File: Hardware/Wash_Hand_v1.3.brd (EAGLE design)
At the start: 71.1 x 48.3 mm, 64 parts, among them IC1 LM358D, IC2 LP298XS, IC3 4050D, J1 I2C, J2 ICSP, J3 SPI, J5 EXT_VCC, J6 6_PIN_SERIAL_CABLEPTH, Q1 16.0 Mhz, U1 328P

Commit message: Board/Schematic: Update to v1.3a.2
Signed-off-by: Konrad Rzeszutek Wilk <konrad@kernel.org>
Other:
- board text added: "v1.3a.2"
- board text removed: "v1.3a.1"
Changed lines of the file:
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@@
 <circle x="6.35" y="37.592" radius="0.254" width="0.254" layer="25"/>
 <circle x="6.35" y="37.592" radius="0.567959375" width="0.1524" layer="25"/>
-<text x="21.336" y="19.558" size="1.778" layer="26" ratio="14" rot="MR0">v1.3a.1</text>
+<text x="21.336" y="19.558" size="1.778" layer="26" ratio="14" rot="MR0">v1.3a.2</text>
 <text x="56.134" y="15.494" size="1.016" layer="25" ratio="14">#
 [  ]
@@
 <element name="MICROSD" library="darnok_microsd" package="114-00841-68" value="114-00841-68" x="9.94" y="29.718" smashed="yes" rot="R270"/>
 <element name="FRAME1" library="darnok_frame" package="REVISION_TEXT" value="" x="54.356" y="22.606" smashed="yes">
-<attribute name="REVISION" value="v1.3a.1" x="54.356" y="22.606" size="1.778" layer="27" display="off"/>
+<attribute name="REVISION" value="v1.3a.2" x="54.356" y="22.606" size="1.778" layer="27" display="off"/>
 </element>
 <element name="FRAME2" library="darnok_frame" package="REVISION_TEXT" value="" x="18.542" y="19.812" smashed="yes" rot="MR0">
-<attribute name="REVISION" value="v1.3a.1" x="18.542" y="19.812" size="1.778" layer="28" rot="MR0" display="off"/>
+<attribute name="REVISION" value="v1.3a.2" x="18.542" y="19.812" size="1.778" layer="28" rot="MR0" display="off"/>
 </element>
 </elements>

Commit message: Board/Schematic: Change 22pf to 10pf
Which makes the crystal work..

Signed-off-by: Konrad Rzeszutek Wilk <konrad@kernel.org>
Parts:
- C1, C2: value 22pF -> 10pF
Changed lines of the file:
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@@
 </autorouter>
 <elements>
-<element name="C1" library="SparkFun-Capacitors" library_urn="urn:adsk.eagle:library:510" package="1206" package3d_urn="urn:adsk.eagle:package:37426/1" value="22pF" x="25.654" y="18.288" smashed="yes" rot="R270">
+<element name="C1" library="SparkFun-Capacitors" library_urn="urn:adsk.eagle:library:510" package="1206" package3d_urn="urn:adsk.eagle:package:37426/1" value="10pF" x="25.654" y="18.288" smashed="yes" rot="R270">
 <attribute name="NAME" x="26.67" y="18.288" size="0.6096" layer="25" font="vector" ratio="20" rot="R270" align="bottom-center"/>
 <attribute name="PROD_ID" value="CAP-10057" x="-28.956" y="-4.572" size="1.778" layer="27" rot="R270" display="off"/>
 <attribute name="VALUE" value="10uF" x="24.638" y="18.288" size="0.6096" layer="27" font="vector" ratio="20" rot="R270" align="top-center"/>
 </element>
-<element name="C2" library="SparkFun-Capacitors" library_urn="urn:adsk.eagle:library:510" package="1206" package3d_urn="urn:adsk.eagle:package:37426/1" value="22pF" x="29.718" y="18.288" smashed="yes" rot="R90">
+<element name="C2" library="SparkFun-Capacitors" library_urn="urn:adsk.eagle:library:510" package="1206" package3d_urn="urn:adsk.eagle:package:37426/1" value="10pF" x="29.718" y="18.288" smashed="yes" rot="R90">
 <attribute name="NAME" x="28.702" y="18.288" size="0.6096" layer="25" font="vector" ratio="20" rot="R90" align="bottom-center"/>
 <attribute name="PROD_ID" value="CAP-10057" x="84.328" y="46.228" size="1.778" layer="27" rot="R90" display="off"/>

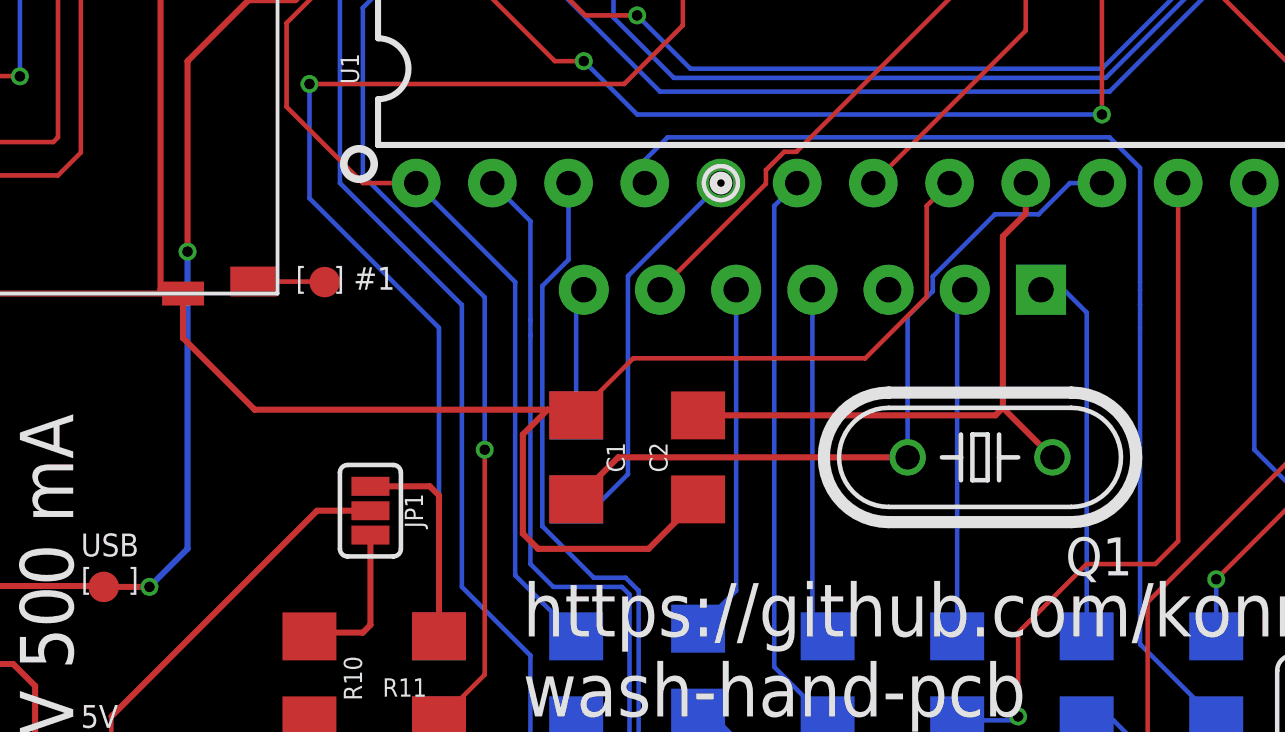
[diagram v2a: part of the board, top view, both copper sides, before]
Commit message: Board/Schematic: Fix the 16MHz/10pF capacitors.
The way they are were in the schematic looked right.
Two capacitors off the crystal. Both capacitors go to
ground. Except that what Eagle decided it should be was:

XTAL1         XTAL2
|             |
+--[CRYSTAL]--+
	 [CAP]
	  |
	 [CAP]
	  |
	 [GND]

Instead of the:

XTAL1         XTAL2
|             |
+--[CRYSTAL]--+
[CAP]        [CAP]
|             |
\------+------/
 [GND]

This fixes it.

Signed-off-by: Konrad Rzeszutek Wilk <konrad@kernel.org>
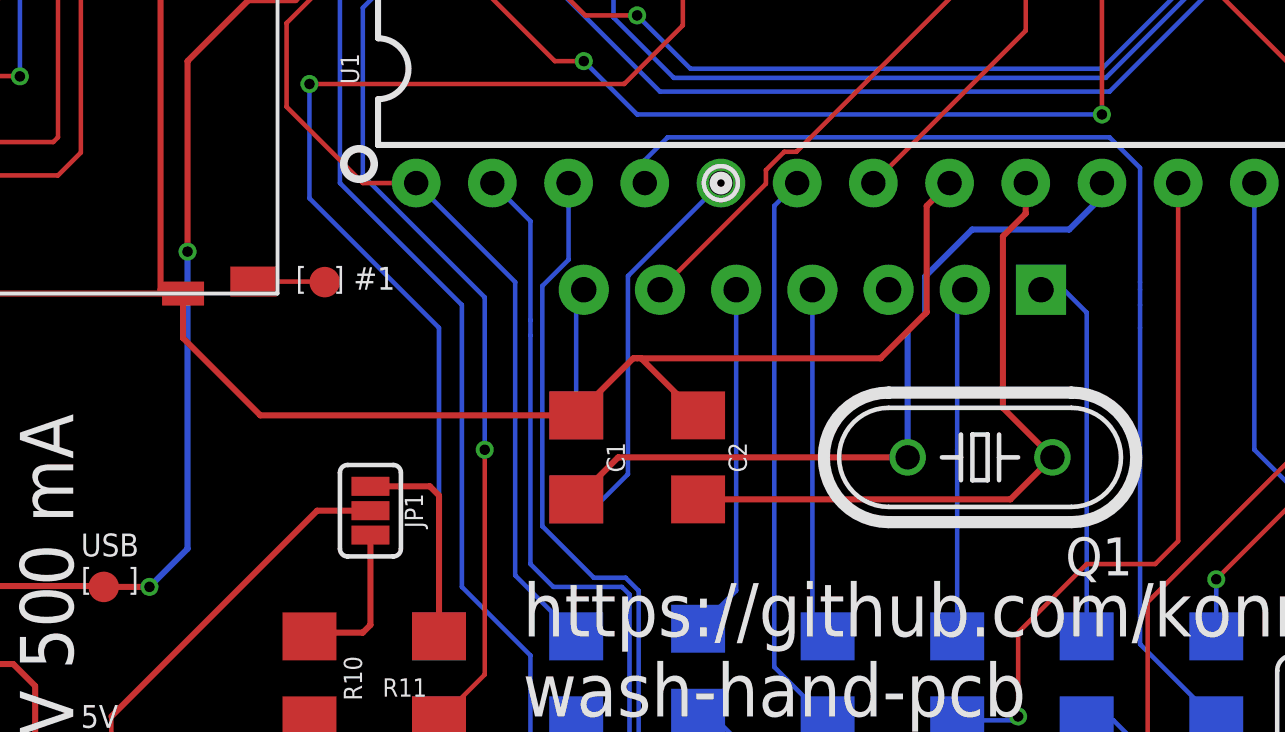
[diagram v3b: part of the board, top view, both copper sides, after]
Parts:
- turned C2 to 270 degrees
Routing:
- net 0: track 346.2 -> 338.0 mm
- net XTAL1: track 20.4 -> 22.5 mm
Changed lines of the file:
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@@
 <attribute name="VALUE" value="10uF" x="24.638" y="18.288" size="0.6096" layer="27" font="vector" ratio="20" rot="R270" align="top-center"/>
 </element>
-<element name="C2" library="SparkFun-Capacitors" library_urn="urn:adsk.eagle:library:510" package="1206" package3d_urn="urn:adsk.eagle:package:37426/1" value="10pF" x="29.718" y="18.288" smashed="yes" rot="R90">
-<attribute name="NAME" x="28.702" y="18.288" size="0.6096" layer="25" font="vector" ratio="20" rot="R90" align="bottom-center"/>
-<attribute name="PROD_ID" value="CAP-10057" x="84.328" y="46.228" size="1.778" layer="27" rot="R90" display="off"/>
-<attribute name="VALUE" value="10uF" x="30.734" y="18.288" size="0.6096" layer="27" font="vector" ratio="20" rot="R90" align="top-center"/>
+<element name="C2" library="SparkFun-Capacitors" library_urn="urn:adsk.eagle:library:510" package="1206" package3d_urn="urn:adsk.eagle:package:37426/1" value="10pF" x="29.718" y="18.288" smashed="yes" rot="R270">
+<attribute name="NAME" x="30.734" y="18.288" size="0.6096" layer="25" font="vector" ratio="20" rot="R270" align="bottom-center"/>
+<attribute name="PROD_ID" value="CAP-10057" x="-24.892" y="-9.652" size="1.778" layer="27" rot="R270" display="off"/>
+<attribute name="VALUE" value="10uF" x="28.702" y="18.288" size="0.6096" layer="27" font="vector" ratio="20" rot="R270" align="top-center"/>
 </element>
 <element name="J" library="SparkFun-Connectors" library_urn="urn:adsk.eagle:library:513" package="1X03" package3d_urn="urn:adsk.eagle:package:38063/1" value="D0    GND  VCC  ," x="63.5" y="8.89" smashed="yes" rot="MR180">
@@
 <signal name="0">
 <contactref element="U$4" pad="5"/>
-<contactref element="C2" pad="1"/>
-<contactref element="C1" pad="1"/>
 <contactref element="J" pad="2"/>
 <contactref element="J5" pad="1"/>
@@
 <wire x1="11.938" y1="23.748" x2="4.7" y2="23.748" width="0.2032" layer="1"/>
 <wire x1="4.7" y1="23.748" x2="4.699" y2="23.749" width="0.2032" layer="1"/>
-<wire x1="14.938840625" y1="19.877" x2="12.55" y2="22.265840625" width="0.2032" layer="1"/>
 <wire x1="12.55" y1="23.748" x2="12.55" y2="22.265840625" width="0.2032" layer="1"/>
 <wire x1="10.033" y1="45.7454" x2="8.763" y2="45.7454" width="0.2032" layer="1"/>
@@
 <wire x1="56.8198" y1="1.1938" x2="47.8282" y2="1.1938" width="0.2032" layer="1"/>
 <wire x1="47.8282" y1="1.1938" x2="45.974" y2="3.048" width="0.2032" layer="1"/>
-<wire x1="14.938840625" y1="19.877" x2="24.703" y2="19.877" width="0.2032" layer="1"/>
-<wire x1="25.465" y1="19.877" x2="25.654" y2="19.688" width="0.2032" layer="1"/>
-<wire x1="29.718" y1="16.888" x2="28.07" y2="15.24" width="0.2032" layer="1"/>
-<wire x1="28.07" y1="15.24" x2="24.384" y2="15.24" width="0.2032" layer="1"/>
-<wire x1="24.384" y1="15.24" x2="23.876" y2="15.748" width="0.2032" layer="1"/>
-<wire x1="23.876" y1="15.748" x2="23.876" y2="19.05" width="0.2032" layer="1"/>
-<wire x1="23.876" y1="19.05" x2="24.703" y2="19.877" width="0.2032" layer="1"/>
-<wire x1="24.703" y1="19.877" x2="25.465" y2="19.877" width="0.2032" layer="1"/>
 <wire x1="45.466" y1="45.85" x2="46.606" y2="45.85" width="0.2032" layer="1"/>
 <wire x1="46.606" y1="45.85" x2="47.752" y2="44.704" width="0.2032" layer="1"/>
@@
 <wire x1="7.874" y1="43.18" x2="10.16" y2="43.18" width="0.2032" layer="1"/>
 <wire x1="4.2" y1="39.506" x2="7.874" y2="43.18" width="0.2032" layer="1"/>
-<wire x1="25.654" y1="19.688" x2="27.556" y2="21.59" width="0.1524" layer="1"/>
-<wire x1="35.2906875" y1="21.59" x2="37.338" y2="23.6373125" width="0.1524" layer="1"/>
-<wire x1="37.338" y1="26.67" x2="38.1" y2="27.432" width="0.1524" layer="1"/>
-<wire x1="27.556" y1="21.59" x2="35.2906875" y2="21.59" width="0.1524" layer="1"/>
-<wire x1="37.338" y1="23.6373125" x2="37.338" y2="26.67" width="0.1524" layer="1"/>
+<wire x1="35.7986875" y1="21.59" x2="37.338" y2="23.1293125" width="0.2032" layer="1"/>
+<wire x1="37.338" y1="26.67" x2="38.1" y2="27.432" width="0.2032" layer="1"/>
+<wire x1="27.816" y1="21.59" x2="35.7986875" y2="21.59" width="0.2032" layer="1"/>
+<wire x1="37.338" y1="23.1293125" x2="37.338" y2="26.67" width="0.2032" layer="1"/>
 <wire x1="16.44076875" y1="39.37" x2="16.316153125" y2="39.494615625" width="0.2032" layer="1"/>
 <wire x1="7.62" y1="4.064" x2="8.636" y2="3.048" width="0.2032" layer="1"/>
@@
 <wire x1="67.37" y1="30.353" x2="69.342" y2="32.325" width="0.2032" layer="1"/>
 <wire x1="69.342" y1="32.325" x2="69.342" y2="34.544" width="0.2032" layer="1"/>
+<contactref element="C2" pad="1"/>
+<contactref element="C1" pad="1"/>
+<wire x1="15.127840625" y1="19.688" x2="25.654" y2="19.688" width="0.2032" layer="1"/>
+<wire x1="12.55" y1="22.265840625" x2="15.127840625" y2="19.688" width="0.2032" layer="1"/>
+<wire x1="25.654" y1="19.688" x2="27.556" y2="21.59" width="0.2032" layer="1"/>
+<wire x1="27.556" y1="21.59" x2="27.686" y2="21.59" width="0.2032" layer="1"/>
+<wire x1="29.718" y1="19.688" x2="27.816" y2="21.59" width="0.2032" layer="1"/>
+<wire x1="27.816" y1="21.59" x2="27.686" y2="21.59" width="0.2032" layer="1"/>
 </signal>
 <signal name="D0">
@@
 <contactref element="C1" pad="2"/>
 <contactref element="Q1" pad="2"/>
-<wire x1="25.654" y1="16.888" x2="27.054" y2="18.288" width="0.2032" layer="1"/>
-<wire x1="27.054" y1="18.288" x2="36.703" y2="18.288" width="0.2032" layer="1"/>
-<wire x1="36.703" y1="18.288" x2="36.703" y2="22.987" width="0.1524" layer="16"/>
-<wire x1="36.703" y1="22.987" x2="37.5412" y2="23.8252" width="0.1524" layer="16"/>
-<wire x1="42.1127625" y1="27.432" x2="43.18" y2="27.432" width="0.1524" layer="16"/>
-<wire x1="41.0713625" y1="26.3906" x2="42.1127625" y2="27.432" width="0.1524" layer="16"/>
-<wire x1="37.5412" y1="24.3178875" x2="39.6139125" y2="26.3906" width="0.1524" layer="16"/>
-<wire x1="39.6139125" y1="26.3906" x2="41.0713625" y2="26.3906" width="0.1524" layer="16"/>
-<wire x1="37.5412" y1="23.8252" x2="37.5412" y2="24.3178875" width="0.1524" layer="16"/>
+<wire x1="36.703" y1="18.288" x2="36.703" y2="22.479" width="0.2032" layer="16"/>
+<wire x1="36.703" y1="22.479" x2="37.2872" y2="23.0632" width="0.1524" layer="16"/>
+<wire x1="43.18" y1="27.432" x2="43.18" y2="26.9752375" width="0.1524" layer="16"/>
+<wire x1="43.18" y1="26.9752375" x2="42.0873625" y2="25.8826" width="0.2032" layer="16"/>
+<wire x1="37.2872" y1="24.3178875" x2="38.8519125" y2="25.8826" width="0.2032" layer="16"/>
+<wire x1="38.8519125" y1="25.8826" x2="42.0873625" y2="25.8826" width="0.2032" layer="16"/>
+<wire x1="37.2872" y1="23.0632" x2="37.2872" y2="24.3178875" width="0.2032" layer="16"/>
+<wire x1="36.703" y1="18.288" x2="27.054" y2="18.288" width="0.2032" layer="1"/>
+<wire x1="27.054" y1="18.288" x2="25.654" y2="16.888" width="0.2032" layer="1"/>
 </signal>
 <signal name="XTAL1">
@@
 <wire x1="39.878" y1="19.939" x2="39.878" y2="25.654" width="0.2032" layer="1"/>
 <wire x1="39.878" y1="25.654" x2="40.64" y2="26.416" width="0.2032" layer="1"/>
-<wire x1="29.718" y1="19.688" x2="39.627" y2="19.688" width="0.2032" layer="1"/>
-<wire x1="39.627" y1="19.688" x2="39.878" y2="19.939" width="0.2032" layer="1"/>
+<wire x1="29.718" y1="16.888" x2="40.129" y2="16.888" width="0.2032" layer="1"/>
+<wire x1="40.129" y1="16.888" x2="41.529" y2="18.288" width="0.2032" layer="1"/>
 </signal>
 <signal name="PIN_C">
